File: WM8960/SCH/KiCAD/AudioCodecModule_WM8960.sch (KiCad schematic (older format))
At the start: 71 parts, among them J1 Line in right filter, J10 Conn_02x06_Top_Bottom, J2 Line in left filter, J3 Line out left, J4 Line out right, J5 Line in right, J6 Line in left, J7 Conn_01x04, J8 Line out, J9 Line in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

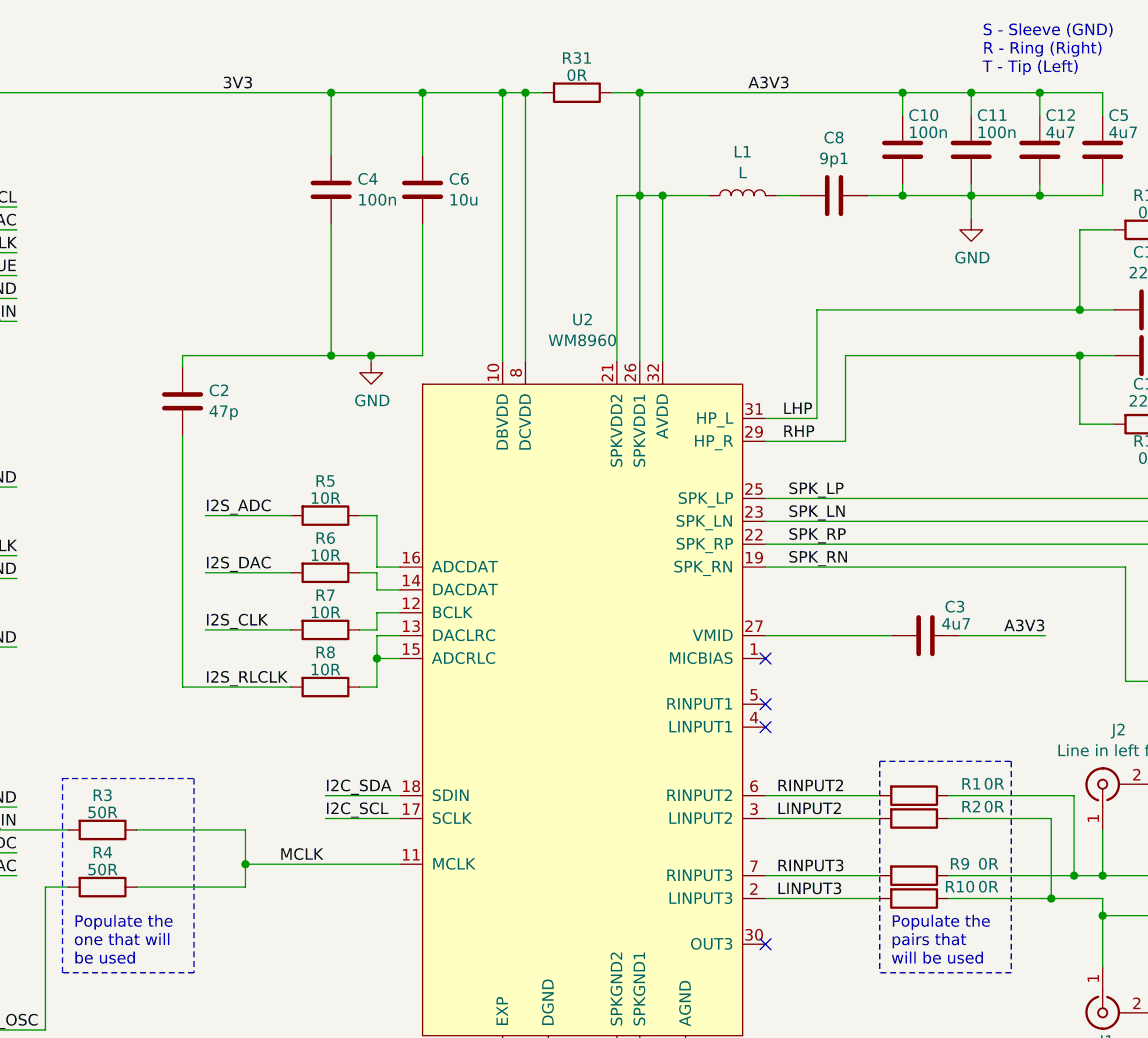
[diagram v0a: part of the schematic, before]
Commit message: WM8960 CODEC schematic ready
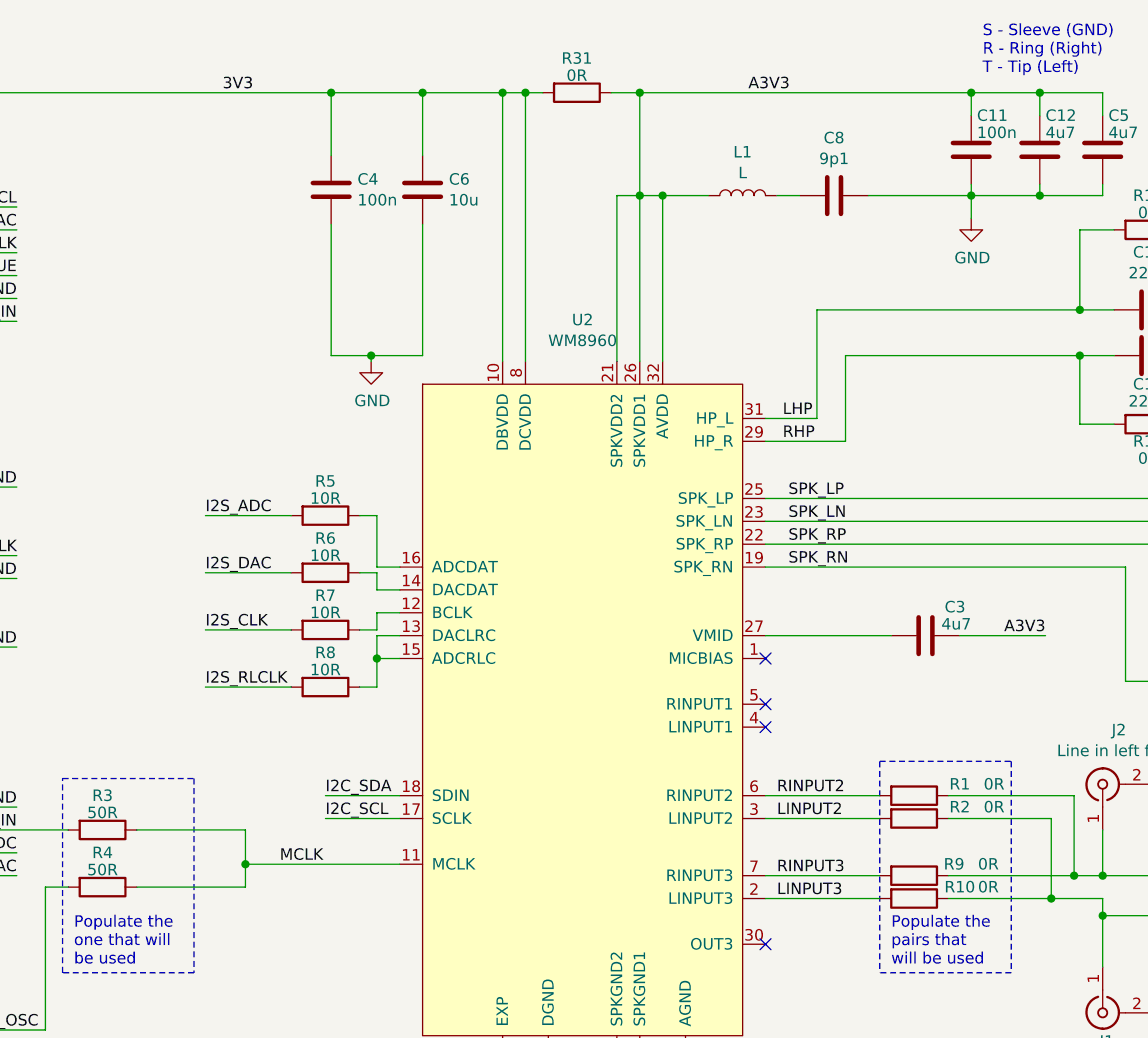
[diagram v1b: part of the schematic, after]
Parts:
- removed C10: 100n, Capacitor_SMD:C_0603_1608Metric_Pad1.05x0.95mm_HandSolder, symbol Device:C
- removed C2: 47p, Capacitor_SMD:C_0603_1608Metric_Pad1.05x0.95mm_HandSolder, symbol Device:C
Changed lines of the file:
@@
-$EndComp
-$Comp
-L Device:C C10
-U 1 1 5FB9E885
-P 6925 1200
-F 0 "C10" H 6900 1050 50  0000 R CNN
-F 1 "100n" H 6900 1125 50  0000 R CNN
-F 2 "Capacitor_SMD:C_0603_1608Metric_Pad1.05x0.95mm_HandSolder" H 6963 1050 50  0001 C CNN
-F 3 "~" H 6925 1200 50  0001 C CNN
-	1    6925 1200
-	-1   0    0    1
 $EndComp
 $Comp
@@
 $EndComp
 Wire Wire Line
-	6775 1400 6925 1400
-Wire Wire Line
 	7525 1400 7525 1350
 Wire Wire Line
@@
 Wire Wire Line
 	7225 1350 7225 1400
-Wire Wire Line
-	6925 1350 6925 1400
-Connection ~ 6925 1400
-Wire Wire Line
-	6925 1400 7225 1400
 Wire Wire Line
 	6475 1400 6375 1400
@@
 Wire Wire Line
 	7225 950  7525 950
-Wire Wire Line
-	6925 1050 6925 950
-Wire Wire Line
-	6925 950  7225 950
 Wire Wire Line
 	4825 1225 4825 950
@@
 	0    1    1    0
 $EndComp
-$Comp
-L Device:C C2
-U 1 1 5FE01F82
-P 3775 2300
-F 0 "C2" H 3660 2254 50  0000 R CNN
-F 1 "47p" H 3660 2345 50  0000 R CNN
-F 2 "Capacitor_SMD:C_0603_1608Metric_Pad1.05x0.95mm_HandSolder" H 3813 2150 50  0001 C CNN
-F 3 "~" H 3775 2300 50  0001 C CNN
-	1    3775 2300
-	-1   0    0    1
-$EndComp
-Wire Wire Line
-	3775 2150 3775 2100
-Wire Wire Line
-	3775 2100 4425 2100
-Connection ~ 4425 2100
-Wire Wire Line
-	3775 2450 3775 3550
-Wire Wire Line
-	3775 3550 4250 3550
+Wire Wire Line
+	3875 3550 4250 3550
 Text Label 4200 4325 0    50   ~ 0
 MCLK
@@
 Wire Wire Line
 	5650 950  5775 950
-Connection ~ 6925 950
 Wire Wire Line
 	5775 1400 5775 950
 Connection ~ 5775 1400
 Connection ~ 5775 950
-Wire Wire Line
-	5775 950  6925 950
 Wire Wire Line
 	5675 2125 5675 1400
@@
 U 1 1 6068F5ED
 P 6975 4025
-F 0 "R1" V 6925 4275 50  0000 C CNN
+F 0 "R1" V 6925 4225 50  0000 C CNN
 F 1 "0R" V 6925 4375 50  0000 C CNN
 F 2 "Resistor_SMD:R_0603_1608Metric_Pad1.05x0.95mm_HandSolder" V 6905 4025 50  0001 C CNN
@@
 U 1 1 6069057E
 P 6975 4125
-F 0 "R2" V 6925 4375 50  0000 C CNN
+F 0 "R2" V 6925 4325 50  0000 C CNN
 F 1 "0R" V 6925 4475 50  0000 C CNN
 F 2 "Resistor_SMD:R_0603_1608Metric_Pad1.05x0.95mm_HandSolder" V 6905 4125 50  0001 C CNN
@@
 U 1 1 60692385
 P 6975 4375
-F 0 "R9" V 6925 4575 50  0000 C CNN
+F 0 "R9" V 6925 4550 50  0000 C CNN
 F 1 "0R" V 6925 4700 50  0000 C CNN
 F 2 "Resistor_SMD:R_0603_1608Metric_Pad1.05x0.95mm_HandSolder" V 6905 4375 50  0001 C CNN
@@
 Text Label 6425 3025 0    50   ~ 0
 SPK_RN
+Wire Wire Line
+	5775 950  7225 950
+Wire Wire Line
+	6775 1400 7225 1400
 $EndSCHEMATC
